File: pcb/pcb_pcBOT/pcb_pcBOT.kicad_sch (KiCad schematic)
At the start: 0 parts

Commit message: pcb
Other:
- added sheet battery (battery.kicad_sch)
- added sheet mortor (dfr.kicad_sch)
- title: schematic_PcBot_2026 -> (none)
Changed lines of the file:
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@@
 (kicad_sch (version 20230121) (generator eeschema)
   (paper "A4")
-  (title_block
-    (title "schematic_PcBot_2026")
-    (rev "1.0")
-  )
-  (sheet (at 30.48 148.59) (size 66.04 40.64) (fields_autoplaced)
+  (sheet (at 27.94 124.46) (size 54.61 57.15) (fields_autoplaced)
     (stroke (width 0.1524) (type solid))
     (fill (color 0 0 0 0.0000))
-    (property "Sheetname" "capteur tof" (at 30.48 147.8784 0)
+    (property "Sheetname" "battery" (at 27.94 123.7484 0)
       (effects (font (size 1.27 1.27)) (justify left bottom))
     )
-    (property "Sheetfile" "tof.kicad_sch" (at 30.48 189.8146 0)
+    (property "Sheetfile" "battery.kicad_sch" (at 27.94 182.1946 0)
+      (effects (font (size 1.27 1.27)) (justify left top))
+    )
+    (instances
+      (project "pcb_pcBOT"
+        (path "/704e4da3-8ee7-458f-8a0f-3fc97e8dc2a6" (page "4"))
+      )
+    )
+  )
+  (sheet (at 101.6 151.13) (size 66.04 40.64) (fields_autoplaced)
+    (stroke (width 0.1524) (type solid))
+    (fill (color 0 0 0 0.0000))
+    (property "Sheetname" "capteur tof" (at 101.6 150.4184 0)
+      (effects (font (size 1.27 1.27)) (justify left bottom))
+    )
+    (property "Sheetfile" "tof.kicad_sch" (at 101.6 192.3546 0)
       (effects (font (size 1.27 1.27)) (justify left top))
     )
@@
       (project "pcb_pcBOT"
         (path "/704e4da3-8ee7-458f-8a0f-3fc97e8dc2a6" (page "5"))
+      )
+    )
+  )
+  (sheet (at 186.69 100.33) (size 86.36 39.37) (fields_autoplaced)
+    (stroke (width 0.1524) (type solid))
+    (fill (color 0 0 0 0.0000))
+    (property "Sheetname" "mortor" (at 186.69 99.6184 0)
+      (effects (font (size 1.27 1.27)) (justify left bottom))
+    )
+    (property "Sheetfile" "dfr.kicad_sch" (at 186.69 140.2846 0)
+      (effects (font (size 1.27 1.27)) (justify left top))
+    )
+    (instances
+      (project "pcb_pcBOT"
+        (path "/704e4da3-8ee7-458f-8a0f-3fc97e8dc2a6" (page "8"))
       )
     )
@@
     )
   )
-  (sheet (at 102.87 72.39) (size 76.2 73.66) (fields_autoplaced)
+  (sheet (at 105.41 71.12) (size 60.96 72.39) (fields_autoplaced)
     (stroke (width 0.1524) (type solid))
     (fill (color 0 0 0 0.0000))
-    (property "Sheetname" "stm32" (at 102.87 71.6784 0)
+    (property "Sheetname" "stm32" (at 105.41 70.4084 0)
       (effects (font (size 1.27 1.27)) (justify left bottom))
     )
-    (property "Sheetfile" "stm32.kicad_sch" (at 102.87 146.6346 0)
+    (property "Sheetfile" "stm32.kicad_sch" (at 105.41 144.0946 0)
       (effects (font (size 1.27 1.27)) (justify left top))
     )
@@
     )
   )
-  (sheet (at 27.94 25.4) (size 58.42 74.93) (fields_autoplaced)
+  (sheet (at 27.94 25.4) (size 53.34 67.31) (fields_autoplaced)
     (stroke (width 0.1524) (type solid))
     (fill (color 0 0 0 0.0000))
@@
       (effects (font (size 1.27 1.27)) (justify left bottom))
     )
-    (property "Sheetfile" "bms.kicad_sch" (at 27.94 100.9146 0)
+    (property "Sheetfile" "bms.kicad_sch" (at 27.94 93.2946 0)
       (effects (font (size 1.27 1.27)) (justify left top))
     )

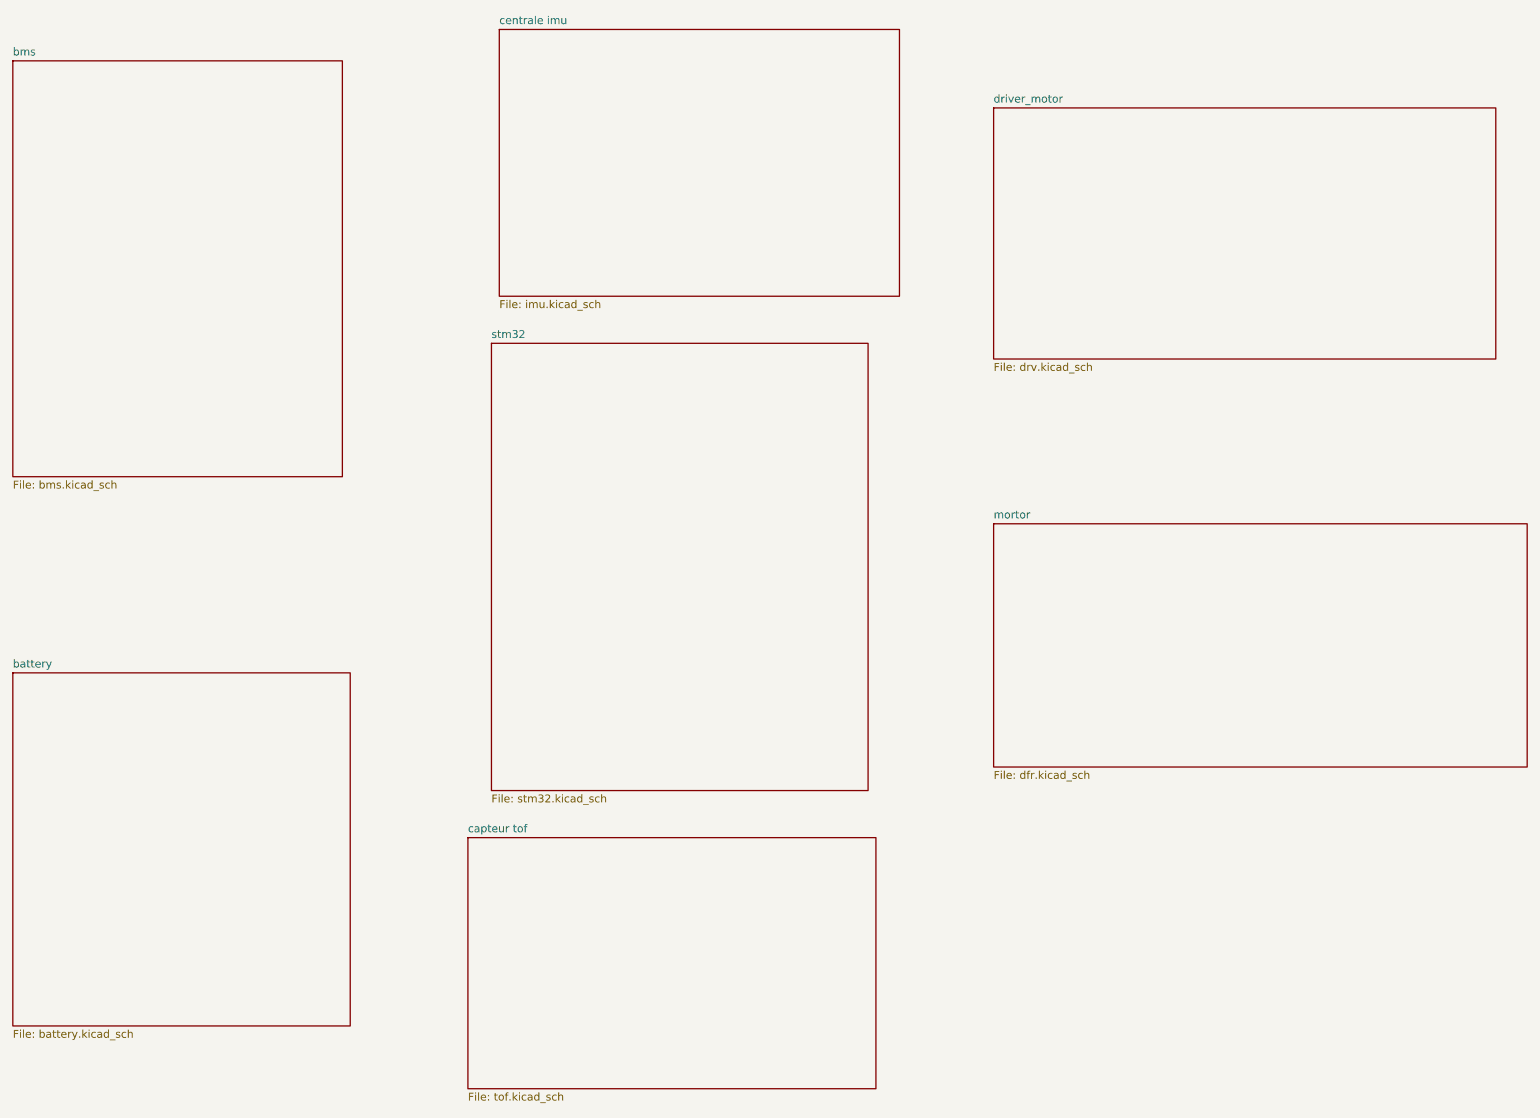
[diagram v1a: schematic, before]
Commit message: ajout de la librairie composant
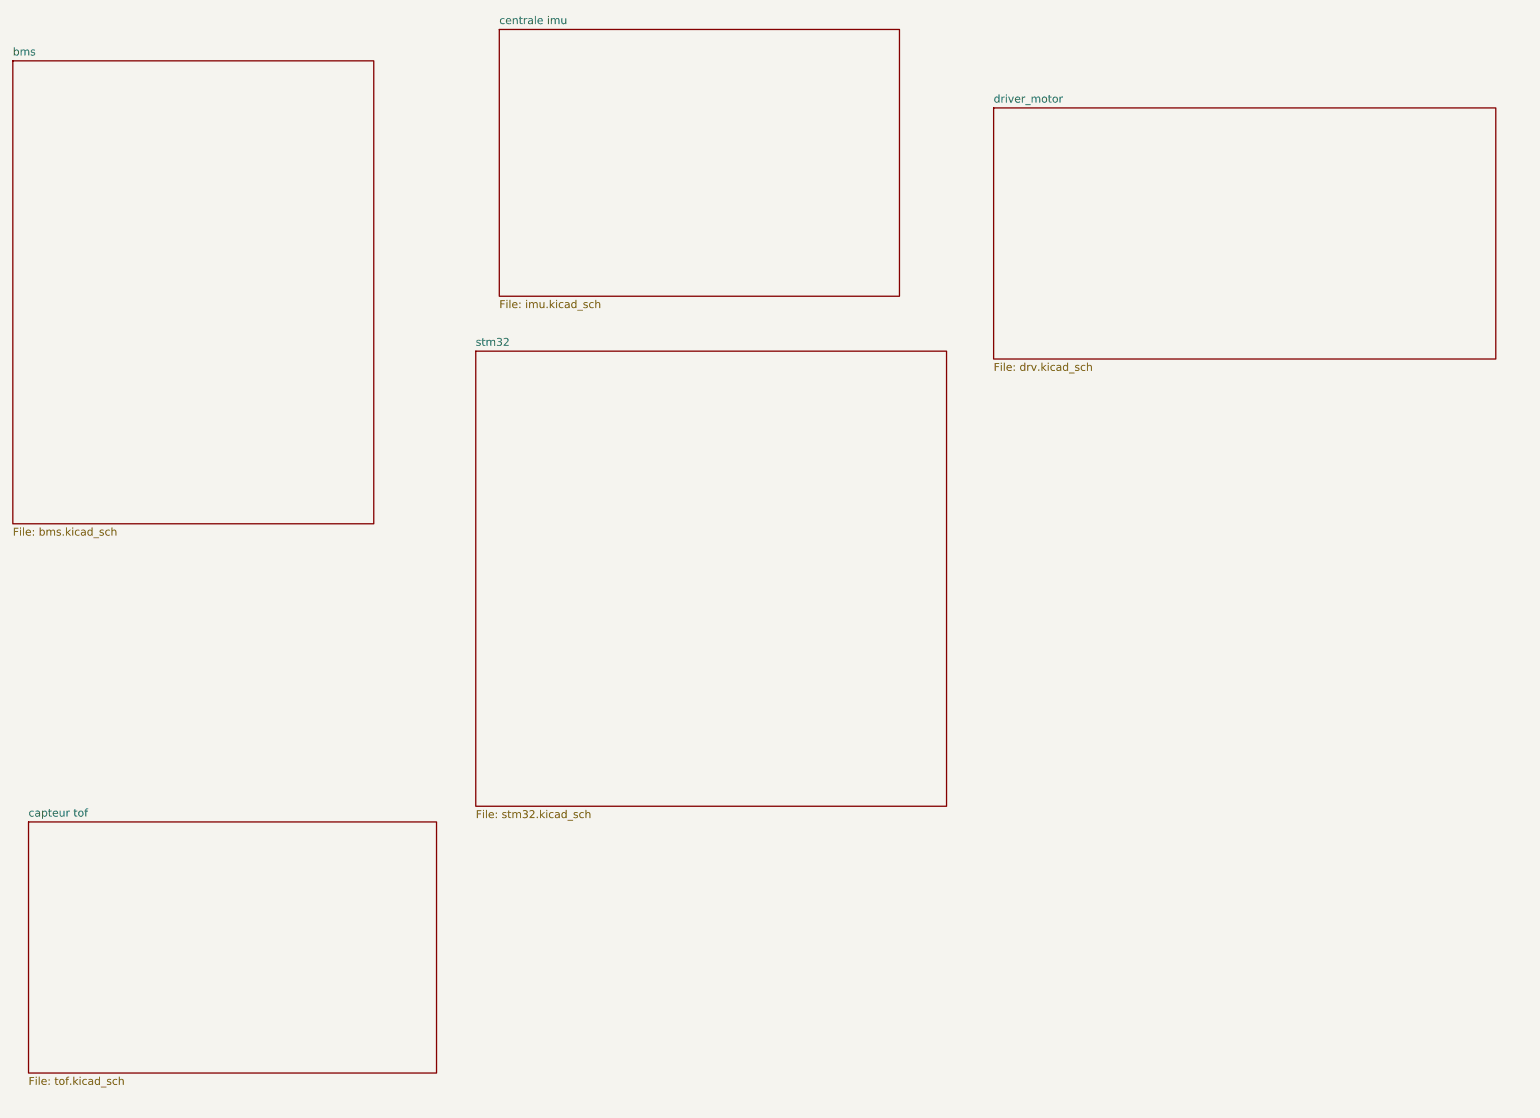
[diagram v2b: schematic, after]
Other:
- removed sheet battery
- removed sheet mortor
- title: (none) -> schematic_PcBot_2026
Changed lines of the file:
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@@
 (kicad_sch (version 20230121) (generator eeschema)
   (paper "A4")
-  (sheet (at 27.94 124.46) (size 54.61 57.15) (fields_autoplaced)
+  (title_block
+    (title "schematic_PcBot_2026")
+    (rev "1.0")
+  )
+  (sheet (at 30.48 148.59) (size 66.04 40.64) (fields_autoplaced)
     (stroke (width 0.1524) (type solid))
     (fill (color 0 0 0 0.0000))
-    (property "Sheetname" "battery" (at 27.94 123.7484 0)
+    (property "Sheetname" "capteur tof" (at 30.48 147.8784 0)
       (effects (font (size 1.27 1.27)) (justify left bottom))
     )
-    (property "Sheetfile" "battery.kicad_sch" (at 27.94 182.1946 0)
-      (effects (font (size 1.27 1.27)) (justify left top))
-    )
-    (instances
-      (project "pcb_pcBOT"
-        (path "/704e4da3-8ee7-458f-8a0f-3fc97e8dc2a6" (page "4"))
-      )
-    )
-  )
-  (sheet (at 101.6 151.13) (size 66.04 40.64) (fields_autoplaced)
-    (stroke (width 0.1524) (type solid))
-    (fill (color 0 0 0 0.0000))
-    (property "Sheetname" "capteur tof" (at 101.6 150.4184 0)
-      (effects (font (size 1.27 1.27)) (justify left bottom))
-    )
-    (property "Sheetfile" "tof.kicad_sch" (at 101.6 192.3546 0)
+    (property "Sheetfile" "tof.kicad_sch" (at 30.48 189.8146 0)
       (effects (font (size 1.27 1.27)) (justify left top))
     )
@@
       (project "pcb_pcBOT"
         (path "/704e4da3-8ee7-458f-8a0f-3fc97e8dc2a6" (page "5"))
-      )
-    )
-  )
-  (sheet (at 186.69 100.33) (size 86.36 39.37) (fields_autoplaced)
-    (stroke (width 0.1524) (type solid))
-    (fill (color 0 0 0 0.0000))
-    (property "Sheetname" "mortor" (at 186.69 99.6184 0)
-      (effects (font (size 1.27 1.27)) (justify left bottom))
-    )
-    (property "Sheetfile" "dfr.kicad_sch" (at 186.69 140.2846 0)
-      (effects (font (size 1.27 1.27)) (justify left top))
-    )
-    (instances
-      (project "pcb_pcBOT"
-        (path "/704e4da3-8ee7-458f-8a0f-3fc97e8dc2a6" (page "8"))
       )
     )
@@
     )
   )
-  (sheet (at 105.41 71.12) (size 60.96 72.39) (fields_autoplaced)
+  (sheet (at 102.87 72.39) (size 76.2 73.66) (fields_autoplaced)
     (stroke (width 0.1524) (type solid))
     (fill (color 0 0 0 0.0000))
-    (property "Sheetname" "stm32" (at 105.41 70.4084 0)
+    (property "Sheetname" "stm32" (at 102.87 71.6784 0)
       (effects (font (size 1.27 1.27)) (justify left bottom))
     )
-    (property "Sheetfile" "stm32.kicad_sch" (at 105.41 144.0946 0)
+    (property "Sheetfile" "stm32.kicad_sch" (at 102.87 146.6346 0)
       (effects (font (size 1.27 1.27)) (justify left top))
     )
@@
     )
   )
-  (sheet (at 27.94 25.4) (size 53.34 67.31) (fields_autoplaced)
+  (sheet (at 27.94 25.4) (size 58.42 74.93) (fields_autoplaced)
     (stroke (width 0.1524) (type solid))
     (fill (color 0 0 0 0.0000))
@@
       (effects (font (size 1.27 1.27)) (justify left bottom))
     )
-    (property "Sheetfile" "bms.kicad_sch" (at 27.94 93.2946 0)
+    (property "Sheetfile" "bms.kicad_sch" (at 27.94 100.9146 0)
       (effects (font (size 1.27 1.27)) (justify left top))
     )
